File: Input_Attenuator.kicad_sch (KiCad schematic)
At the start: 5 parts, among them U3 OPA1679

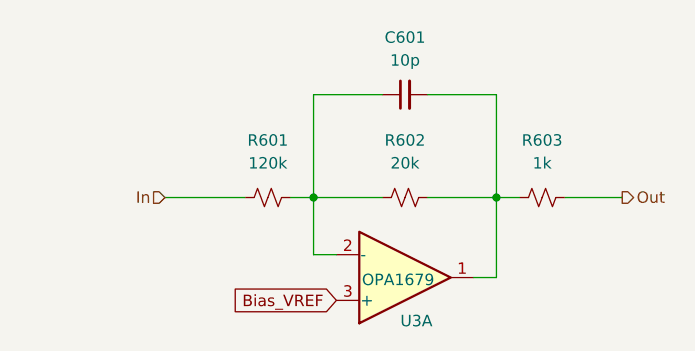
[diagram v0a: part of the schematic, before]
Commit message: Added 33R resistors to SDOUT
Added 33R resistors to SDOUT to decrease slew rate slightly to reduce radiated emissions.
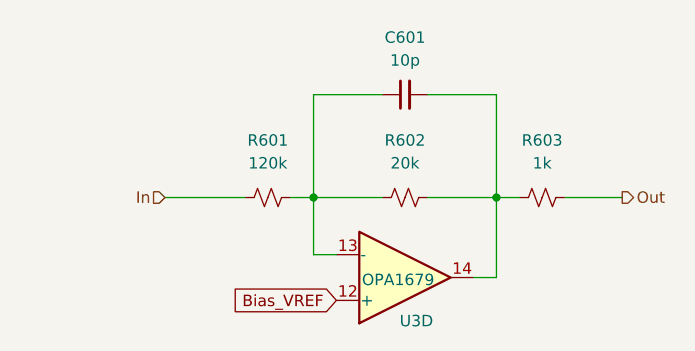
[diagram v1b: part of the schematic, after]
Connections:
- net Bias_VREF: now also U3.12 (+); no longer U3.3 (+)
- net at C601.2, R602.2, R603.1: now also U3.14; no longer U3.1
- net at C601.1, R601.2, R602.1: now also U3.13 (-); no longer U3.2 (-)
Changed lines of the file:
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@@
 		(lib_id "Decapod_Devices:TL074")
 		(at 137.16 95.25 0)
-		(unit 1)
+		(unit 4)
 		(exclude_from_sim no)
 		(in_bom yes)

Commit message: Version 1 ready to order
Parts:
- R601: LCSC (none) -> C25808
- R602: LCSC (none) -> C4184
- R603: LCSC (none) -> C21190
- U3: LCSC (none) -> C2057264
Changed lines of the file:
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@@
 		(shape output)
 		(at 162.56 86.36 0)
-		(fields_autoplaced yes)
 		(effects
 			(font
@@
 		(shape input)
 		(at 111.76 86.36 180)
-		(fields_autoplaced yes)
 		(effects
 			(font
@@
 		(property "MPN" "OPA1679"
 			(at 143.51 102.87 0)
+			(effects
+				(font
+					(size 1.27 1.27)
+				)
+				(hide yes)
+			)
+		)
+		(property "LCSC" "C2057264"
+			(at 137.16 95.25 0)
 			(effects
 				(font
@@
 			)
 		)
+		(property "LCSC" " C21190"
+			(at 153.67 86.36 0)
+			(effects
+				(font
+					(size 1.27 1.27)
+				)
+				(hide yes)
+			)
+		)
 		(pin "2"
 		)
@@
 			)
 		)
+		(property "LCSC" " C4184"
+			(at 138.43 86.36 0)
+			(effects
+				(font
+					(size 1.27 1.27)
+				)
+				(hide yes)
+			)
+		)
 		(pin "2"
 		)
@@
 			(at 123.19 86.36 0)
 			(effects
+				(font
+					(size 1.27 1.27)
+				)
+				(hide yes)
+			)
+		)
+		(property "LCSC" "C25808"
+			(at 123.19 86.36 0)
+			(effects
